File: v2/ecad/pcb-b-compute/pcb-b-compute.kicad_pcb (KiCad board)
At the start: 4 copper layers, 245 x 170 mm, 161 parts, among them Q1 2N7002 (SOT-23) OnOff open-dr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, U1 FE1.1s, U10 TPS22810DRV, U11 INA219AIDCN, U12 USBLC6-2SC6, U13 TPS22810DRV, U14 INA219AIDCN, U15 TPS22810DRV, U16 INA219AIDCN, U17 USBLC6-2SC6, U18 TPS22810DRV, U19 INA219AIDCN, U2 USBLC6-2SC6, U20 PCA9555PW, U3 USBLC6-2SC6, U4 TPS2065CDBV, U5 INA219AIDCN, U6 USBLC6-2SC6, U7 TPS2065CDBV, U8 INA219AIDCN, U9 USBLC6-2SC6, Y1 12 MHz 3225

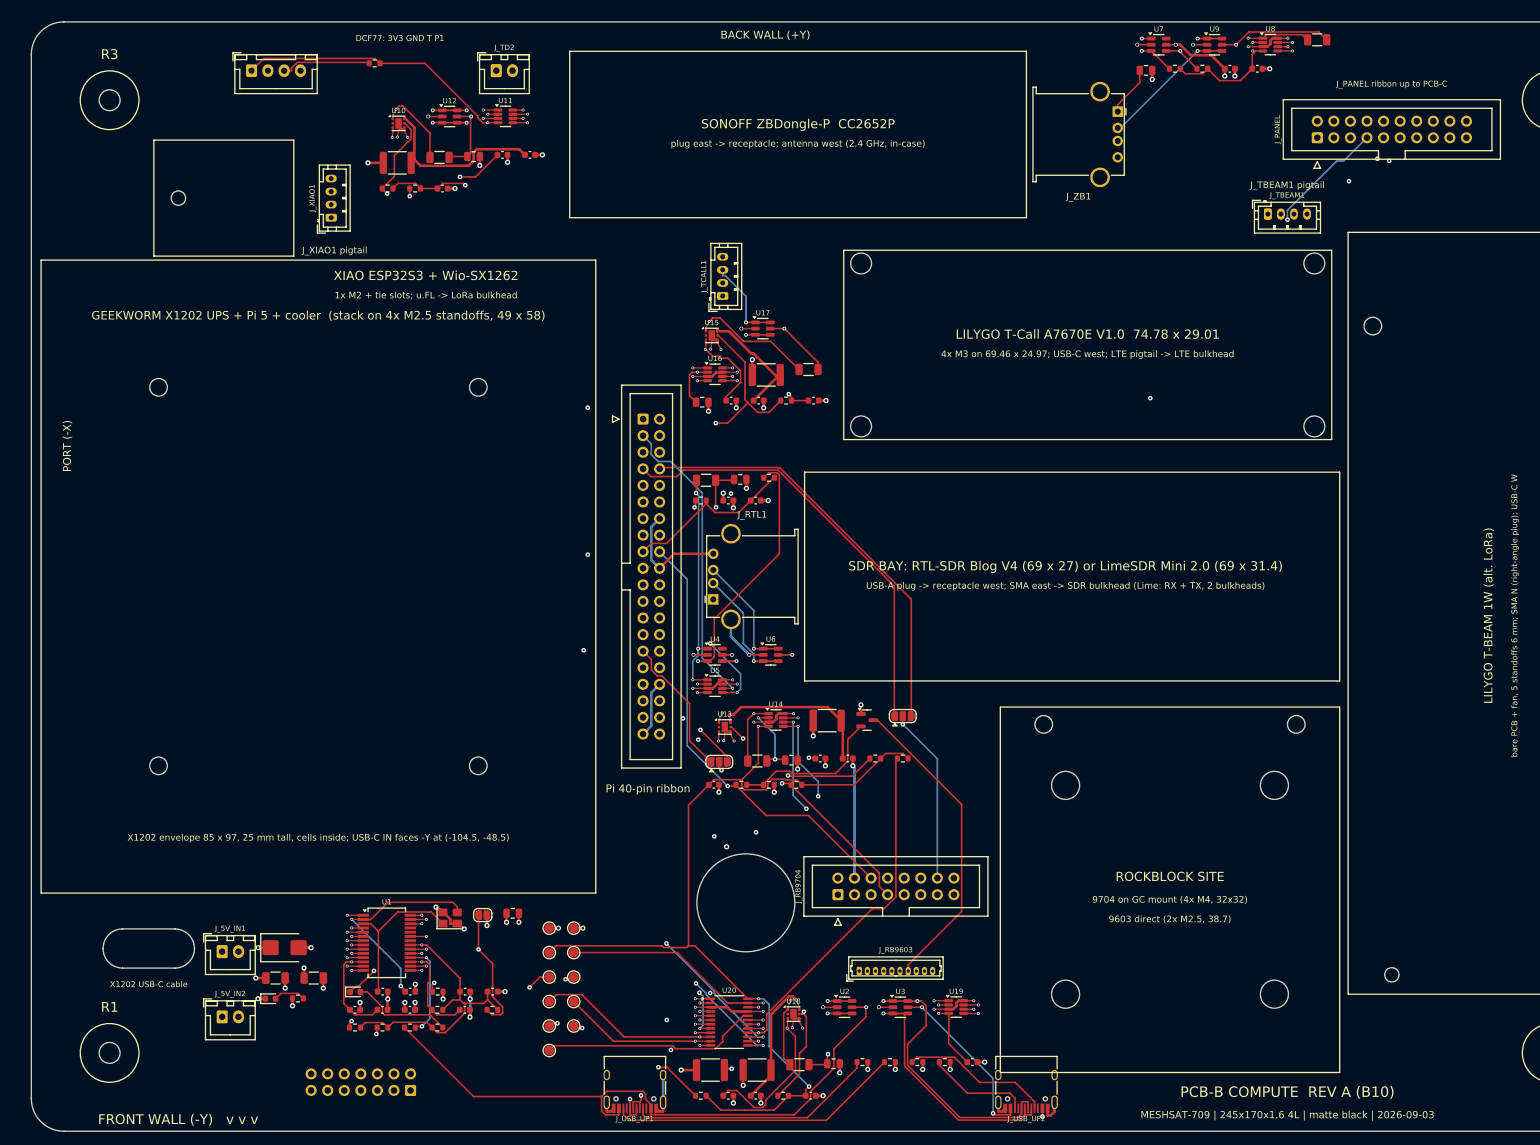
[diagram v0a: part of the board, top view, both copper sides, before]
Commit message: chore(ecad): A17 and B11 project files as routed and finished [MESHSAT-709]
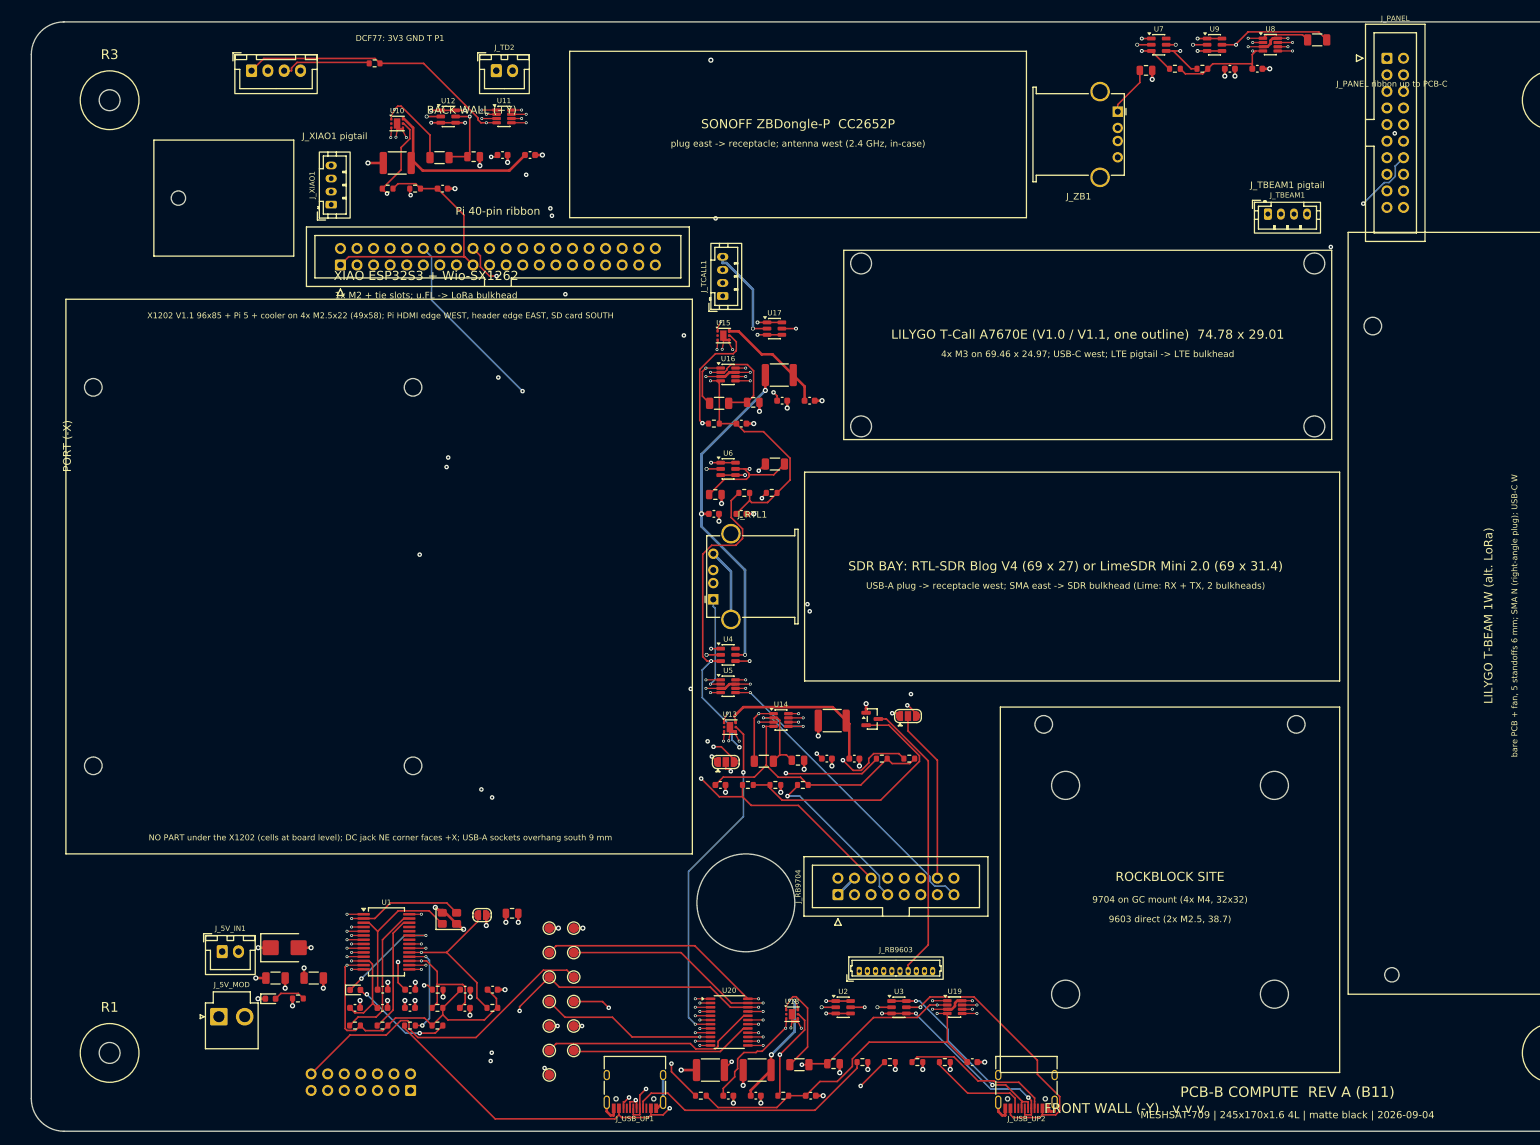
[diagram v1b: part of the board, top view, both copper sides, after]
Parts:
- removed J_5V_IN2: X1202 5V OUT (XH2.54), JST_XH_B2B-XH-A_1x02_P2.50mm_Vertical
- added J_5V_MOD: 5 V module rail from PCB-A J_5V_MOD1 (JST-VH, 18 AWG): + -, JST_VH_B2P-VH_1x02_P3.96mm_Vertical, F.Cu at (56.2, 177.4)
- added TP12: EXP_SPARE5, TestPoint_Pad_D1.5mm, F.Cu at (110.6, 182.6)
- added TP13: PI_GPIO_SPARE1, TestPoint_Pad_D1.5mm, F.Cu at (106.9, 186.4)
- J_5V_IN1: value X1202 5V OUT (XH2.54) -> X1202 5 V OUT sense (XH2.54): enables the module-rail boost on PCB-A over J_AB1.12, 110k load only
- moved J_GPIO1 52.0 mm to (74.9, 62.3), turned to 90 degrees
- moved U6 29.2 mm to (134.3, 93.5)
- moved J_PANEL 16.2 mm to (235.2, 30.6), turned to 0 degrees
- moved R22 14.6 mm to (132.9, 83.5)
- moved S_ZB1 12.0 mm to (140.0, 57.5)
- moved S_ZB3 12.0 mm to (140.0, 28.0)
- moved R34 11.6 mm to (132.1, 86.6)
- moved C21 11.6 mm to (136.3, 86.6)
- moved R30 10.9 mm to (141.0, 97.2)
- moved R14 10.8 mm to (141.5, 92.8)
- moved H5 10.0 mm to (37.0, 139.0)
- moved H6 10.0 mm to (37.0, 81.0)
- moved H7 10.0 mm to (86.0, 139.0)
- moved H8 10.0 mm to (86.0, 81.0)
- moved C20 7.81 mm to (142.6, 83.0)
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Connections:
- J_5V_IN1 pad 1: +5V -> /X1202_5V
- J_AB1 pad 12: /BANK_ALERT -> /X1202_5V
- J_GPIO1 pad 11: /BANK_ALERT -> /PI_GPIO_SPARE1
- U20 pad 17: /BANK_ALERT -> /EXP_SPARE5
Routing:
- net /BANK_ALERT: track 158.7 -> 0.00 mm, vias 2 -> 0
- net /PI_GPIO_SPARE1: track 0.00 -> 132.1 mm, vias 0 -> 2
- net /RB_STATUS: track 85.8 -> 168.6 mm
- net /UART0_RX: track 46.7 -> 122.3 mm, vias 1 -> 2
- net /RB_IEN: track 46.3 -> 115.3 mm, vias 0 -> 1
- net /EXP_INT: track 290.6 -> 359.4 mm, vias 3 -> 4
- net /TR_APRS: track 241.7 -> 307.6 mm, vias 2 -> 0
- net /SDA: track 469.1 -> 533.8 mm, vias 9 -> 8
- net /UART2_RX: track 21.7 -> 85.4 mm, vias 0 -> 1
- net /RB_CTRL: track 68.2 -> 130.5 mm, vias 1 -> 2
- net /UART0_TX: track 64.9 -> 126.7 mm, vias 0 -> 2
- net /RB_XMTG: track 76.1 -> 136.6 mm, vias 1 -> 2
- net /RB_NETAV: track 97.2 -> 156.8 mm, vias 0 -> 1
- net /UART2_TX: track 66.6 -> 125.4 mm, vias 0 -> 2
- net +3V3: track 603.8 -> 660.6 mm, vias 14 -> 11
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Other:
- outline, holes or cut-outs redrawn
- board text added: "LILYGO T-Call A7670E (V1.0 / V1.1, one outline) 74.78 x 29.01"
- board text added: "MESHSAT-709 | 245x170x1.6 4L | matte black | 2026-09-04"
- board text added: "NO PART under the X1202 (cells at board level); DC jack NE corner faces +X; USB-A sockets overhang south 9 mm"
- board text added: "PCB-B COMPUTE REV A (B11)"
- board text added: "X1202 V1.1 96x85 + Pi 5 + cooler on 4x M2.5x22 (49x58); Pi HDMI edge WEST, header edge EAST, SD card SOUTH"
- board text removed: "GEEKWORM X1202 UPS + Pi 5 + cooler (stack on 4x M2.5 standoffs, 49 x 58)"
- board text removed: "LILYGO T-Call A7670E V1.0 74.78 x 29.01"
- board text removed: "MESHSAT-709 | 245x170x1.6 4L | matte black | 2026-09-03"
- board text removed: "PCB-B COMPUTE REV A (B10)"
- board text removed: "X1202 USB-C cable"
- board text removed: "X1202 envelope 85 x 97, 25 mm tall, cells inside; USB-C IN faces -Y at (-104.5, -48.5)"

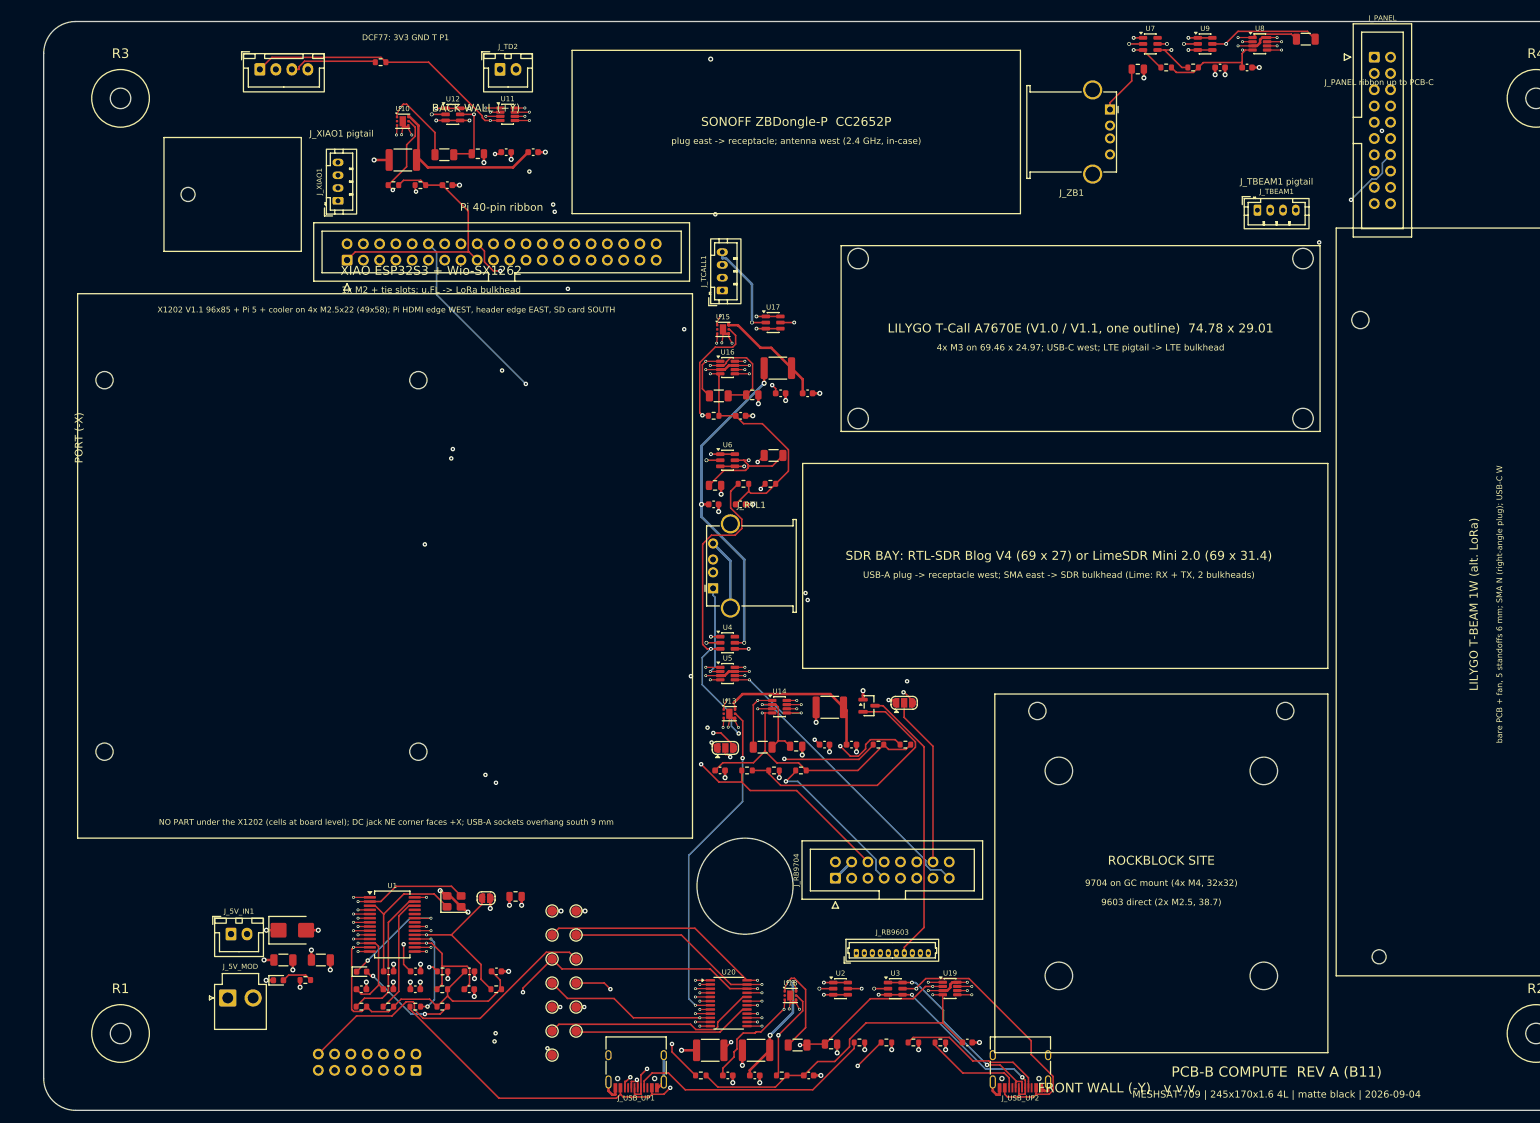
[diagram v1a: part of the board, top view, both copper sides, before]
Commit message: feat(release): PCB-B B12 routed clean (0 hard, 0 unrouted), no X1202, three rails from PCB-A, deliverable [MESHSAT-790]
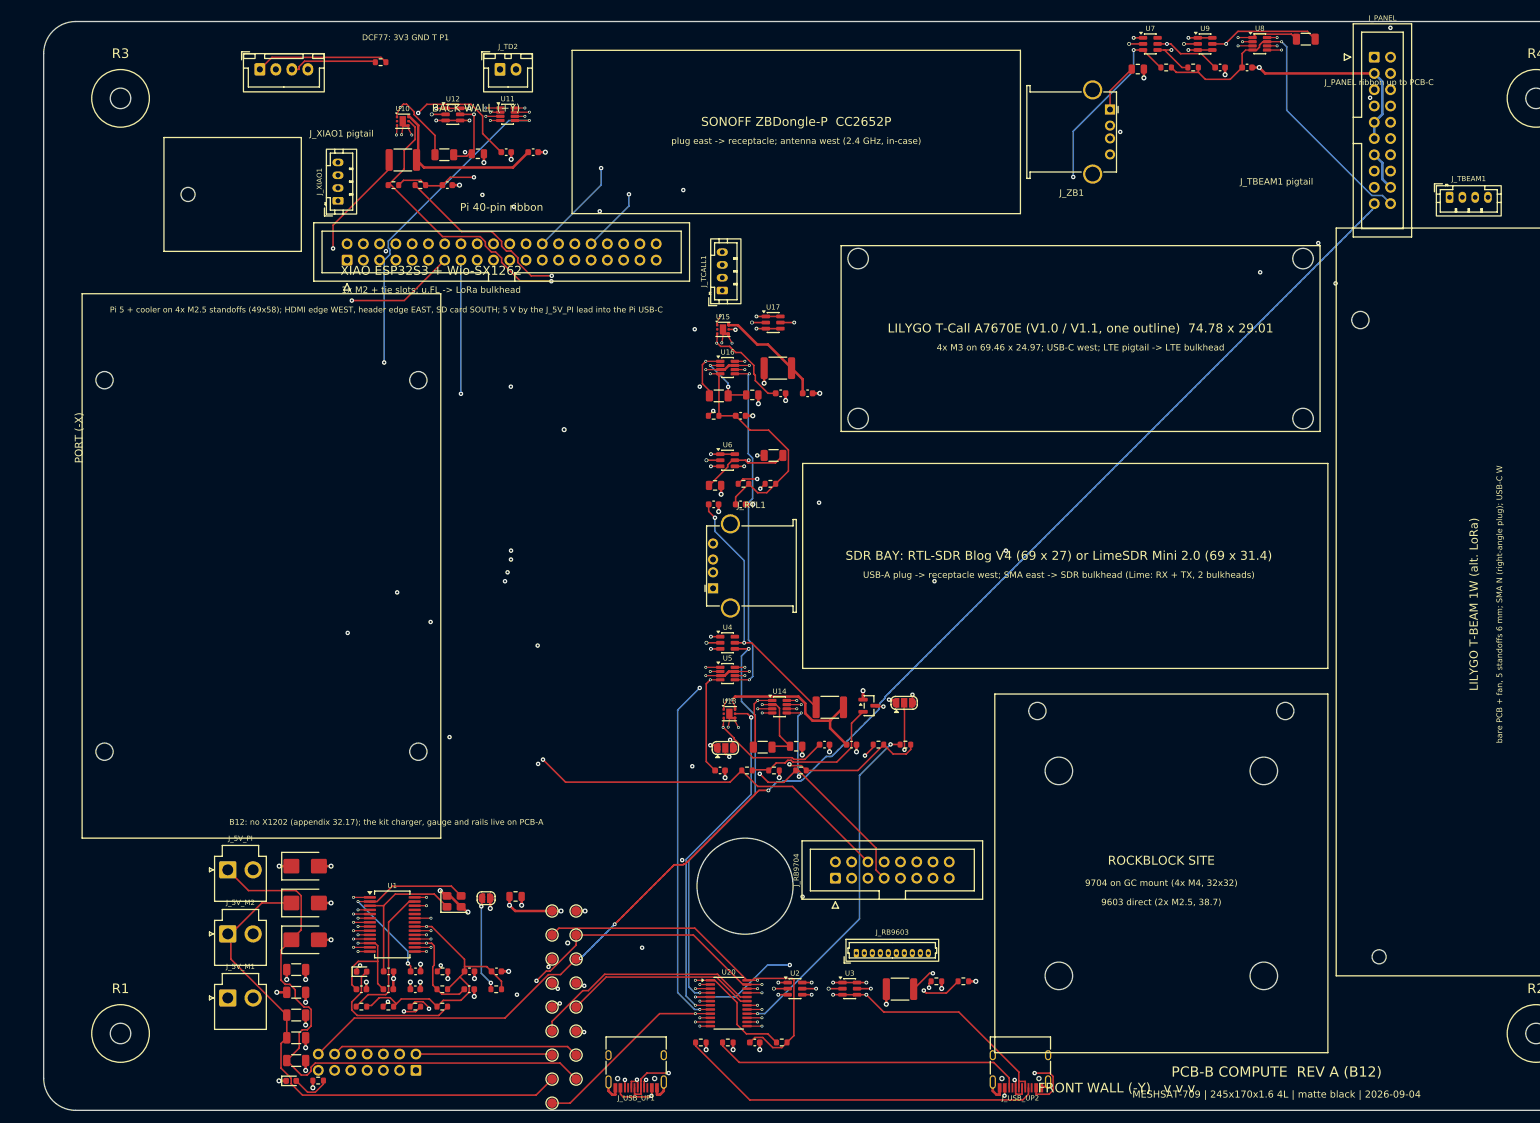
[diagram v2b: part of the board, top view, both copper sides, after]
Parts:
- removed C23: 1n, C_0603_1608Metric
- removed C24: 100n, C_0603_1608Metric
- removed C25: 10u, C_0805_2012Metric
- removed C32: 1u, C_0603_1608Metric
- removed F3: 1.1A hold 1812, Fuse_1812_4532Metric
- removed J_5V_IN1: X1202 5 V OUT sense (XH2.54): enables the module-rail boost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, JST_XH_B2B-XH-A_1x02_P2.50mm_Vertical
- removed J_5V_MOD: 5 V module rail from PCB-A J_5V_MOD1 (JST-VH, 18 AWG): + -, JST_VH_B2P-VH_1x02_P3.96mm_Vertical
- removed R24: 0.05R 1% 1206, R_1206_3216Metric
- removed R35: 100k, R_0603_1608Metric
- removed U18: TPS22810DRV, WSON-6-1EP_2x2mm_P0.65mm_EP1x1.6mm
- removed U19: INA219AIDCN, SOT-23-8
- added C40: 100u 10V, C_1206_3216Metric, F.Cu at (66.9, 180.1)
- added C41: 100u 10V, C_1206_3216Metric, F.Cu at (66.9, 183.7)
- added C42: 100u 10V, C_1206_3216Metric, F.Cu at (66.9, 187.2)
- added D3: SMBJ5.0A, D_SMB, F.Cu at (68.3, 162.6)
- added D4: SMBJ5.0A, D_SMB, F.Cu at (68.3, 168.4)
- added J_5V_M1: 5 V rail M1 from PCB-A J_5V_M1 (JST-VH, 18 AWG): + - ; hub,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, JST_VH_B2P-VH_1x02_P3.96mm_Vertical, F.Cu at (56.2, 177.4)
- added J_5V_M2: 5 V rail M2 from PCB-A J_5V_M2 (JST-VH, 18 AWG): + - ; SDR,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, JST_VH_B2P-VH_1x02_P3.96mm_Vertical, F.Cu at (56.2, 167.4)
- added J_5V_PI: Pi rail 5.1 V 5 A from PCB-A J_5V_PI (JST-VH, 18 AWG): + - 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, JST_VH_B2P-VH_1x02_P3.96mm_Vertical, F.Cu at (56.2, 157.4)
- added TP14: AB_SPARE, TestPoint_Pad_D1.5mm, F.Cu at (110.6, 186.4)
- added TP15: +5V_M2, TestPoint_Pad_D1.5mm, F.Cu at (106.9, 190.1)
- added TP16: +5V_PI, TestPoint_Pad_D1.5mm, F.Cu at (110.6, 190.1)
- added TP17: EXP_SPARE6, TestPoint_Pad_D1.5mm, F.Cu at (106.9, 193.9)
- H5, H6, H7, H8: value M2.5 standoff, Pi/X1202 stack -> M2.5 standoff, Pi 5
- TP13: value PI_GPIO_SPARE1 -> PI_KILL
- moved C26 33.2 mm to (138.5, 184.4)
- moved R11 33.2 mm to (130.1, 184.4)
- moved R12 33.2 mm to (134.3, 184.4)
- moved F6 31.1 mm to (161.2, 176.1)
- moved J_TBEAM1 30.1 mm to (247.0, 52.5)
- moved LED1 15.8 mm to (66.1, 190.4)
- moved R1 15.8 mm to (70.4, 190.4)
- moved R10 15.3 mm to (171.1, 174.9)
- moved R9 15.3 mm to (166.9, 174.9)
- moved R25 13.6 mm to (142.7, 184.4)
- moved D1 10.2 mm to (68.3, 156.9)
- moved U3 7.11 mm to (153.3, 176.0)
- moved U2 7.11 mm to (144.8, 176.0)
- moved C2 6.35 mm to (66.9, 176.6)
- moved C1 2.50 mm to (66.9, 173.0)
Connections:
- C33 pad 1: +5V -> /+5V_M2
- C34 pad 1: +5V -> /+5V_M2
- F4 pad 1: +5V -> /+5V_M2
- F5 pad 1: +5V -> /+5V_M2
- J_AB1 pad 1: /5V_A -> /PI_SHDN_REQ
- J_AB1 pad 12: /X1202_5V -> /AB_SPARE
- J_AB1 pad 2: /5V_A -> /PI_KILL
- J_GPIO1 pad 11: /PI_GPIO_SPARE1 -> /PI_KILL
- J_GPIO1 pad 31: (no net) -> /PI_SHDN_REQ
- TP13 pad 1: /PI_GPIO_SPARE1 -> /PI_KILL
- U20 pad 9: /EN_A -> /EXP_SPARE6
- U4 pad 5: +5V -> /+5V_M2
- U7 pad 5: +5V -> /+5V_M2
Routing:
- net /+5V_M2: track 0.00 -> 446.2 mm, vias 0 -> 5
- net /PI_KILL: track 0.00 -> 157.7 mm
- net /PI_SHDN_REQ: track 0.00 -> 148.6 mm
- net /PI_GPIO_SPARE1: track 132.1 -> 0.00 mm, vias 2 -> 0
- net +5V: track 468.1 -> 361.2 mm, vias 18 -> 12
- net /+5V_PI: track 0.00 -> 93.3 mm
- net /5V_A: track 89.2 -> 0.00 mm, vias 2 -> 0
- net /TX_INHIBIT_n: track 298.1 -> 219.1 mm, vias 0 -> 3
- net /SDA: track 533.8 -> 460.8 mm
- net /PANEL_5V: track 238.1 -> 178.1 mm
- net /EN_TC: track 167.1 -> 116.4 mm, vias 2 -> 4
- net /USB_XIAO_P: track 280.8 -> 326.7 mm, vias 3 -> 4
- net /USB_XIAO_N: track 274.0 -> 318.4 mm, vias 3 -> 5
- net /SW_A: track 42.1 -> 0.00 mm, vias 2 -> 0
- net +3V3: track 660.6 -> 618.9 mm
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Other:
- board text added: "B12: no X1202 (appendix 32.17); the kit charger, gauge and rails live on PCB-A"
- board text added: "J_5V_M1 / J_5V_M2 / J_5V_PI (VH): three rails from PCB-A"
- board text added: "PCB-B COMPUTE REV A (B12)"
- board text added: "Pi 5 + cooler on 4x M2.5 standoffs (49x58); HDMI edge WEST, header edge EAST, SD card SOUTH; 5 V by the J_5V_PI lead into the Pi USB-C"
- board text removed: "J_5V_IN XH"
- board text removed: "NO PART under the X1202 (cells at board level); DC jack NE corner faces +X; USB-A sockets overhang south 9 mm"
- board text removed: "PCB-B COMPUTE REV A (B11)"
- board text removed: "X1202 V1.1 96x85 + Pi 5 + cooler on 4x M2.5x22 (49x58); Pi HDMI edge WEST, header edge EAST, SD card SOUTH"
